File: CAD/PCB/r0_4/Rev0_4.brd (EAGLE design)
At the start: 99 x 79.2 mm, 45 parts, among them IC1 EEPROM, U1 ARDUINO_SHIELDNOHOLESORLABELS

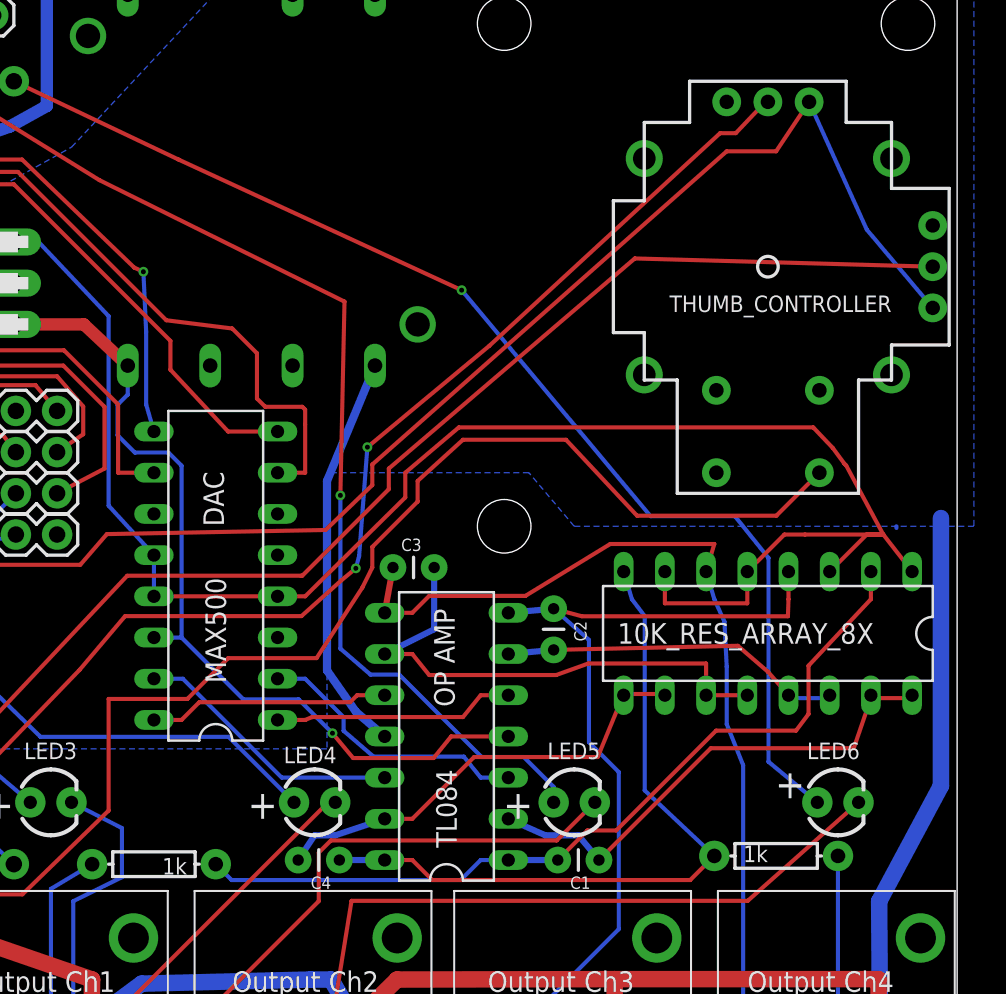
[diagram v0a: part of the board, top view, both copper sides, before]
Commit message: -Added license to each script -Updated syntax for sending custom pulse trains in C++ API to match MATLAB API -Added revised PCB design files to account for longer op amp package (TI replaces ST microsystems)
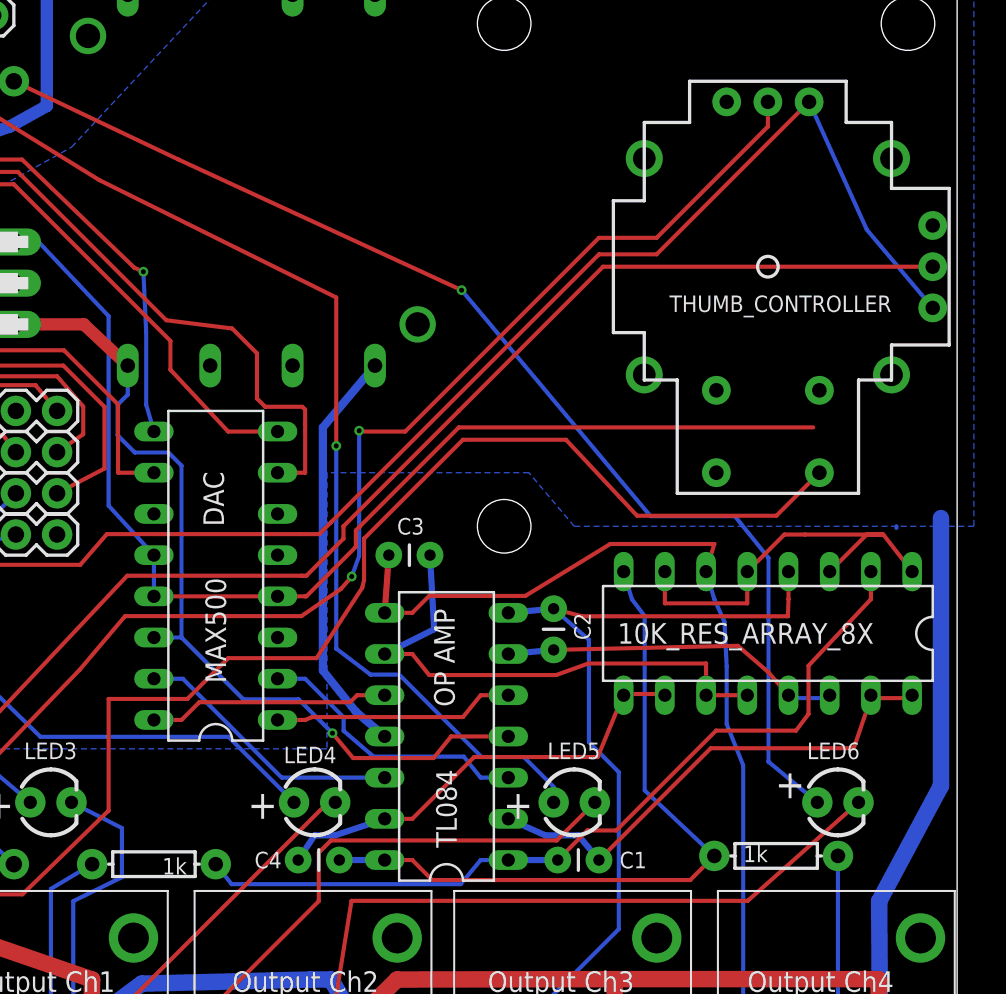
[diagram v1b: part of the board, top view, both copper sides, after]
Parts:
- moved C3 0.80 mm to (64.0, 74.9)
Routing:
- net N$29: track 105.3 -> 97.2 mm
- net N$15: track 75.0 -> 77.6 mm
- net N$45: track 32.3 -> 33.0 mm
- net N$23: track 24.8 -> 25.6 mm
- net N$34: track 65.2 -> 65.9 mm

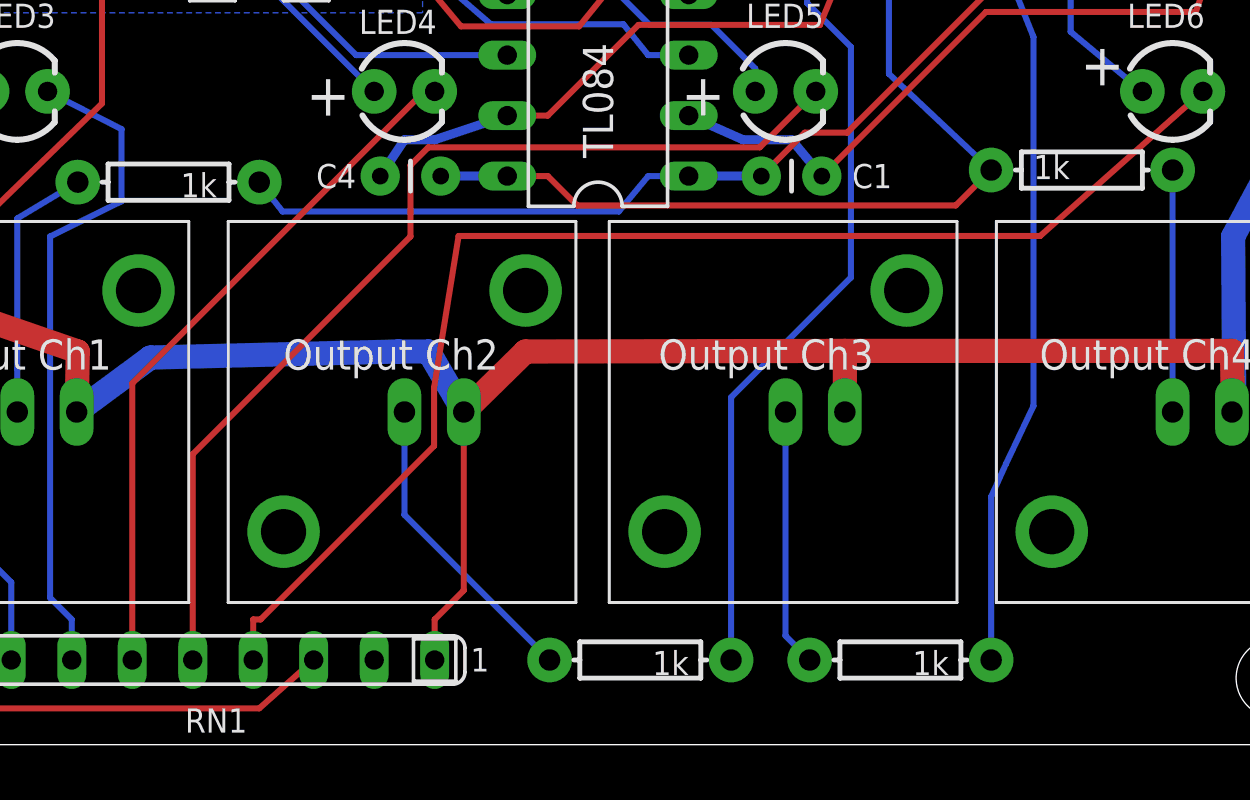
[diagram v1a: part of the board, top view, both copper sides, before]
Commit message: Changed output channel series resistors in CAD files from 1k to 750-ohm (current-limits outputs to a max of 10mA, previously 8.6mA)
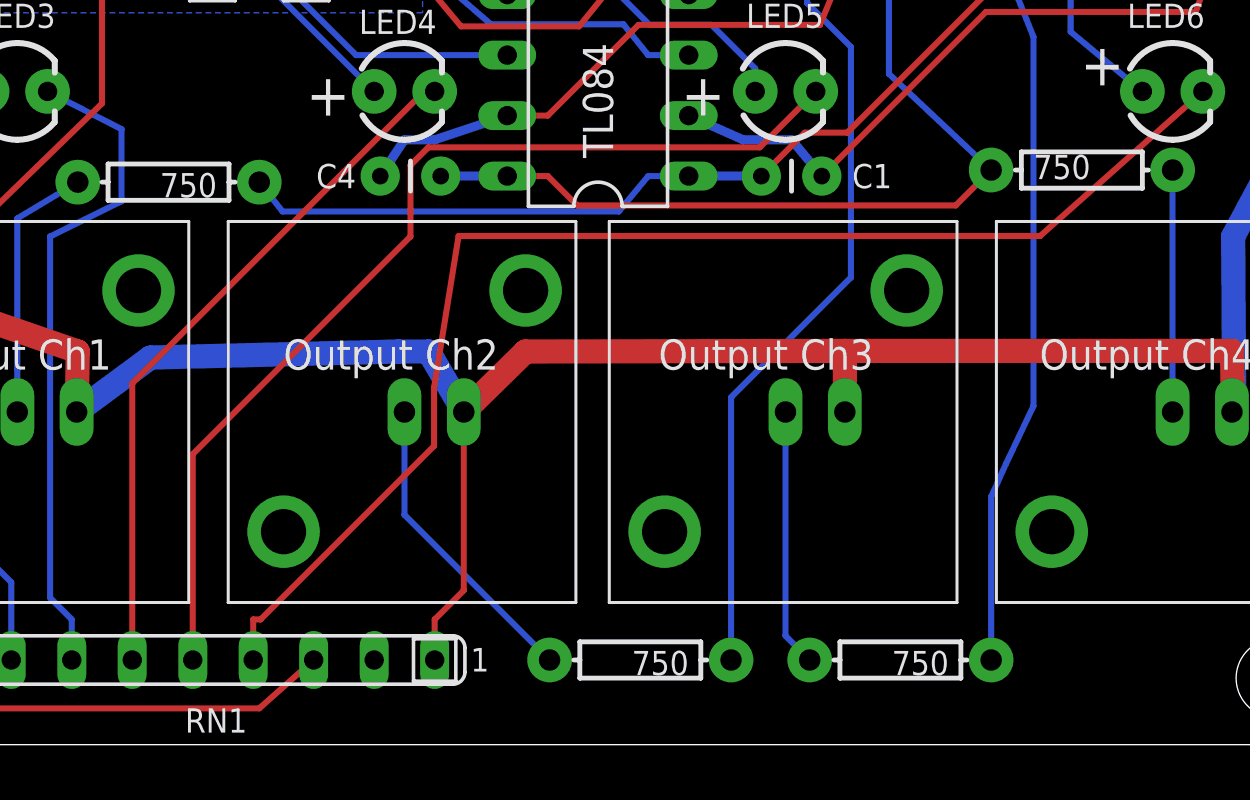
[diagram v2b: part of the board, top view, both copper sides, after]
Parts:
- R6, R7, R8, R9: value 1k -> 750
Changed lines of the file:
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@@
 <attribute name="VALUE" x="54.356" y="34.544" size="1.27" layer="27" ratio="10" rot="R180"/>
 </element>
-<element name="R6" library="SparkFun" package="AXIAL-0.3" value="1k" x="49.53" y="55.88" smashed="yes" rot="R180">
+<element name="R6" library="SparkFun" package="AXIAL-0.3" value="750" x="49.53" y="55.88" smashed="yes" rot="R180">
 <attribute name="VALUE" x="51.562" y="56.261" size="1.016" layer="21" font="vector" ratio="15" rot="R180"/>
 </element>
-<element name="R7" library="SparkFun" package="AXIAL-0.3" value="1k" x="69.342" y="35.814" smashed="yes" rot="R180">
+<element name="R7" library="SparkFun" package="AXIAL-0.3" value="750" x="69.342" y="35.814" smashed="yes" rot="R180">
 <attribute name="VALUE" x="71.374" y="36.195" size="1.016" layer="21" font="vector" ratio="15" rot="R180"/>
 </element>
-<element name="R8" library="SparkFun" package="AXIAL-0.3" value="1k" x="80.264" y="35.814" smashed="yes" rot="R180">
+<element name="R8" library="SparkFun" package="AXIAL-0.3" value="750" x="80.264" y="35.814" smashed="yes" rot="R180">
 <attribute name="VALUE" x="82.296" y="36.195" size="1.016" layer="21" font="vector" ratio="15" rot="R180"/>
 </element>
-<element name="R9" library="SparkFun" package="AXIAL-0.3" value="1k" x="87.884" y="56.388" smashed="yes">
+<element name="R9" library="SparkFun" package="AXIAL-0.3" value="750" x="87.884" y="56.388" smashed="yes">
 <attribute name="VALUE" x="85.852" y="56.007" size="1.016" layer="21" font="vector" ratio="15"/>
 </element>

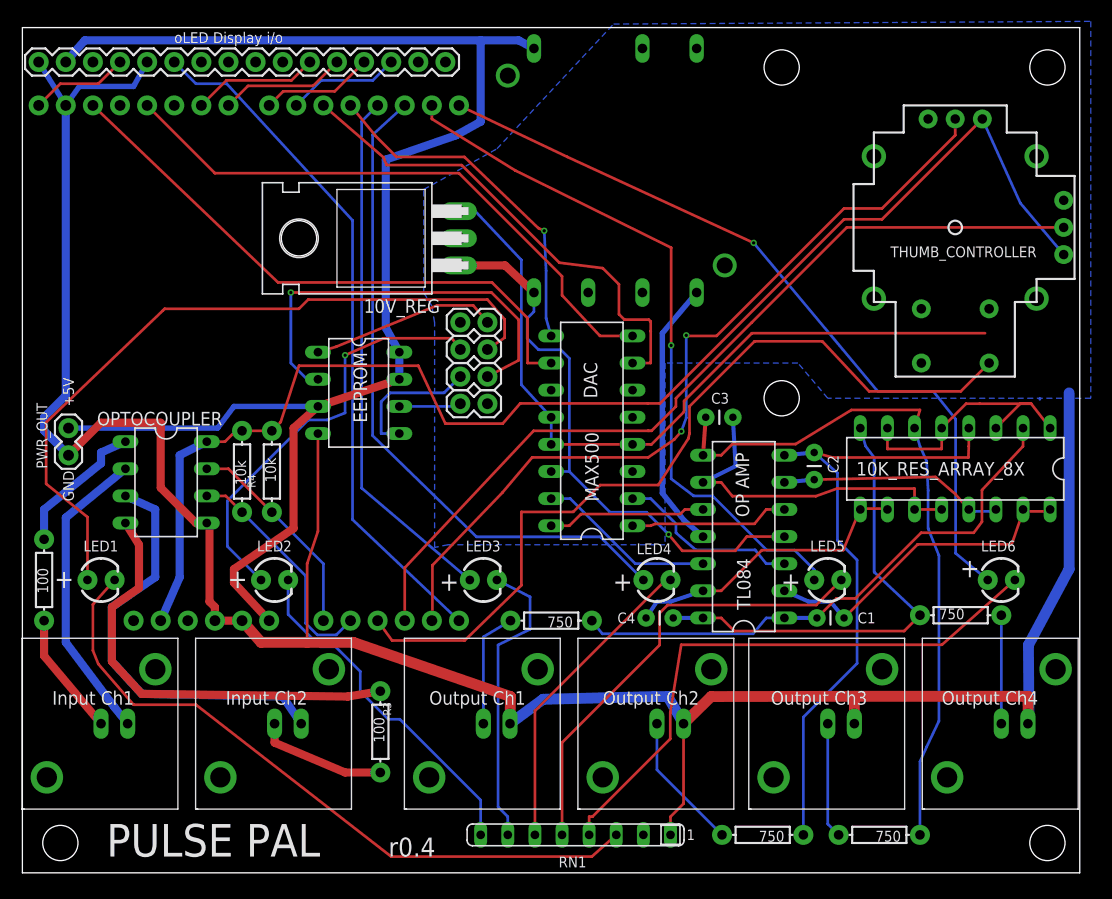
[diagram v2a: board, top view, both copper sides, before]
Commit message: Replaced bipolar voltage converter in PCB design (and BOM) with a lower power, lower cost, more available part from the same family.
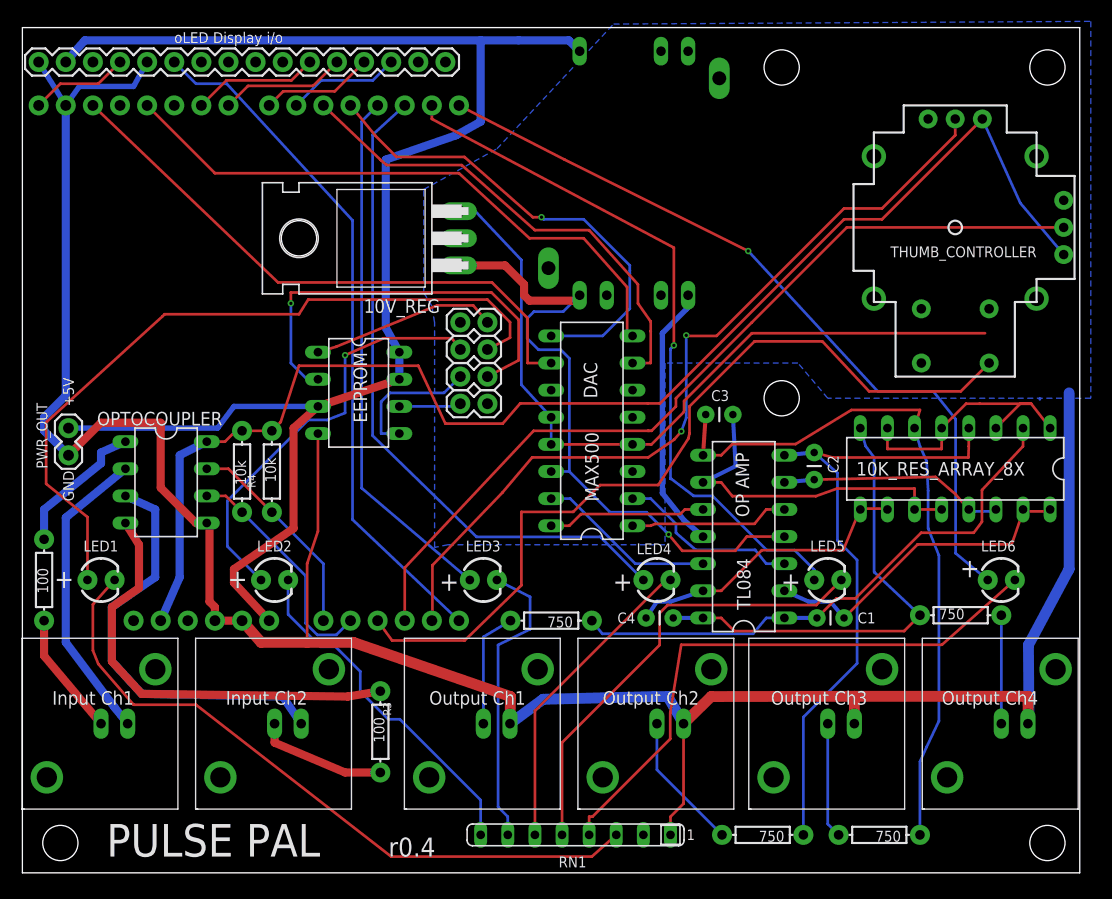
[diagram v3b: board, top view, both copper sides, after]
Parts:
- removed U$7: TDK_LAMBDA_5_TO_BIPOLAR12V, JoshParts:TDK_LAMBDA_5V_TO_BIPOLAR12V
- added U$8: TDK_LAMBDA_5_TO_BI_12_125MA, JoshParts:TDK_LAMBDA_5_TO_BI_12_125MA
- moved C3 0.25 mm to (64.0, 75.2)
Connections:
- net GND: now also U$8.P$2, U$8.P$3, U$8.P$5; no longer U$7.P$2, U$7.P$3, U$7.P$5
- net N$23: now also U$8.P$4; no longer U$7.P$4
- net N$28: now also U$8.P$7; no longer U$7.P$7
- net VCC: now also U$8.P$1; no longer U$7.P$1
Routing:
- net N$8: track 33.0 -> 44.8 mm
- net N$28: track 53.5 -> 62.1 mm
- net VCC: track 140.8 -> 145.4 mm
- net N$5: track 55.5 -> 56.8 mm
- net N$36: track 68.7 -> 69.5 mm

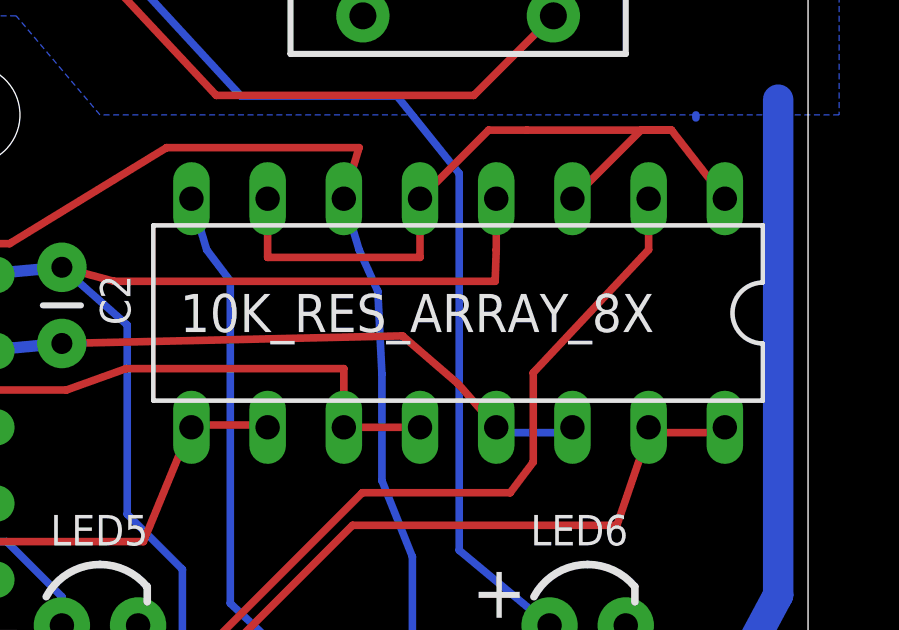
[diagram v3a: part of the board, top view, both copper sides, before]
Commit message: -Cleaned up schematic (preliminary - final version will require re-routing the board)
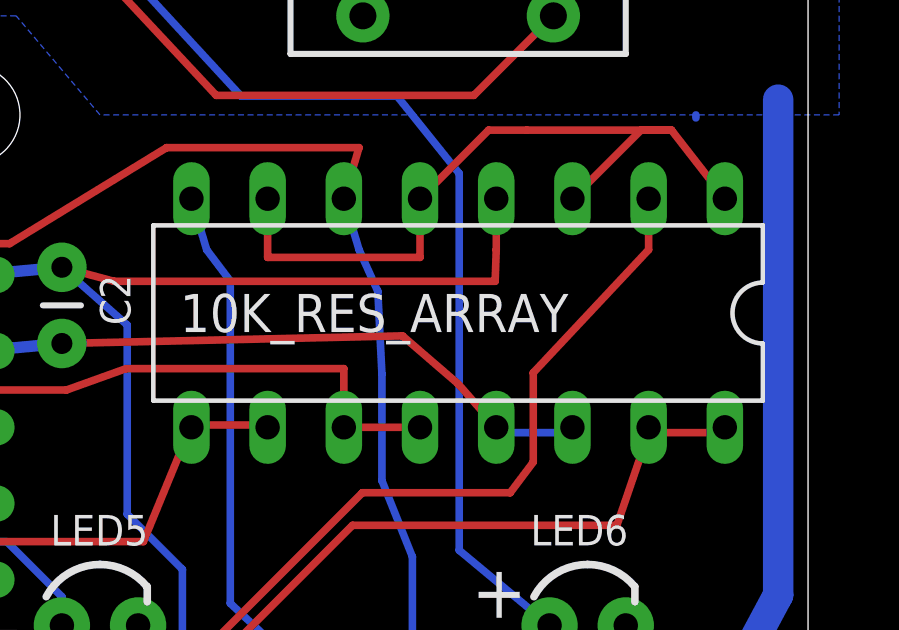
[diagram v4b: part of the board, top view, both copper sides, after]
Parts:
- renumbered 10K_RES_ARRAY_8X to 10K_RES_ARRAY, JP1 to OLED, U1 to MAPLE

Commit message: Since update to  CC3-0512DF-E voltage converter, schematic contained an air-wire. This is now routed. Added schematic graphic of essential circuit for reading triggers and generating outputs.
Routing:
- net N$29: track 97.2 -> 107.1 mm
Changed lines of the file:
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@@
 <wire x1="0" y1="32.258" x2="99.04" y2="32.258" width="0" layer="20"/>
 <wire x1="99.04" y1="32.258" x2="99.04" y2="111.43" width="0" layer="20"/>
-<text x="34.29" y="33.782" size="1.778" layer="21" font="vector">r0.4</text>
+<text x="35.306" y="34.036" size="1.778" layer="21" font="vector">r0.4</text>
 <text x="14.224" y="109.982" size="1.016" layer="21" font="vector">oLED Display i/o</text>
 <text x="2.794" y="48.006" size="1.27" layer="21" font="vector">Input Ch1</text>
@@
 <text x="53.848" y="76.708" size="1.27" layer="21" font="vector" rot="R90">DAC</text>
 <text x="66.802" y="71.628" size="1.27" layer="21" font="vector" rot="R270">OP AMP</text>
-<text x="7.874" y="33.782" size="3.048" layer="21" font="vector">PULSE PAL</text>
+<text x="6.858" y="33.782" size="3.302" layer="21" font="vector">PULSE PAL</text>
 <text x="4.826" y="58.928" size="1.778" layer="21" rot="MR0">+</text>
 <text x="21.082" y="58.928" size="1.778" layer="21" rot="MR0">+</text>
@@
 <wire x1="61.976" y1="76.454" x2="62.23" y2="76.708" width="0.254" layer="1"/>
 <wire x1="62.23" y1="76.708" x2="68.326" y2="82.804" width="0.254" layer="1"/>
-<wire x1="90.17" y1="82.804" x2="89.662" y2="76.2" width="0" layer="19" extent="1-1"/>
+<wire x1="90.17" y1="82.804" x2="93.472" y2="82.804" width="0.254" layer="1"/>
+<wire x1="93.472" y1="82.804" x2="93.472" y2="76.2" width="0.254" layer="1"/>
 </signal>
 <signal name="N$24">
